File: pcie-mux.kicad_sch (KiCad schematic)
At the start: 0 parts

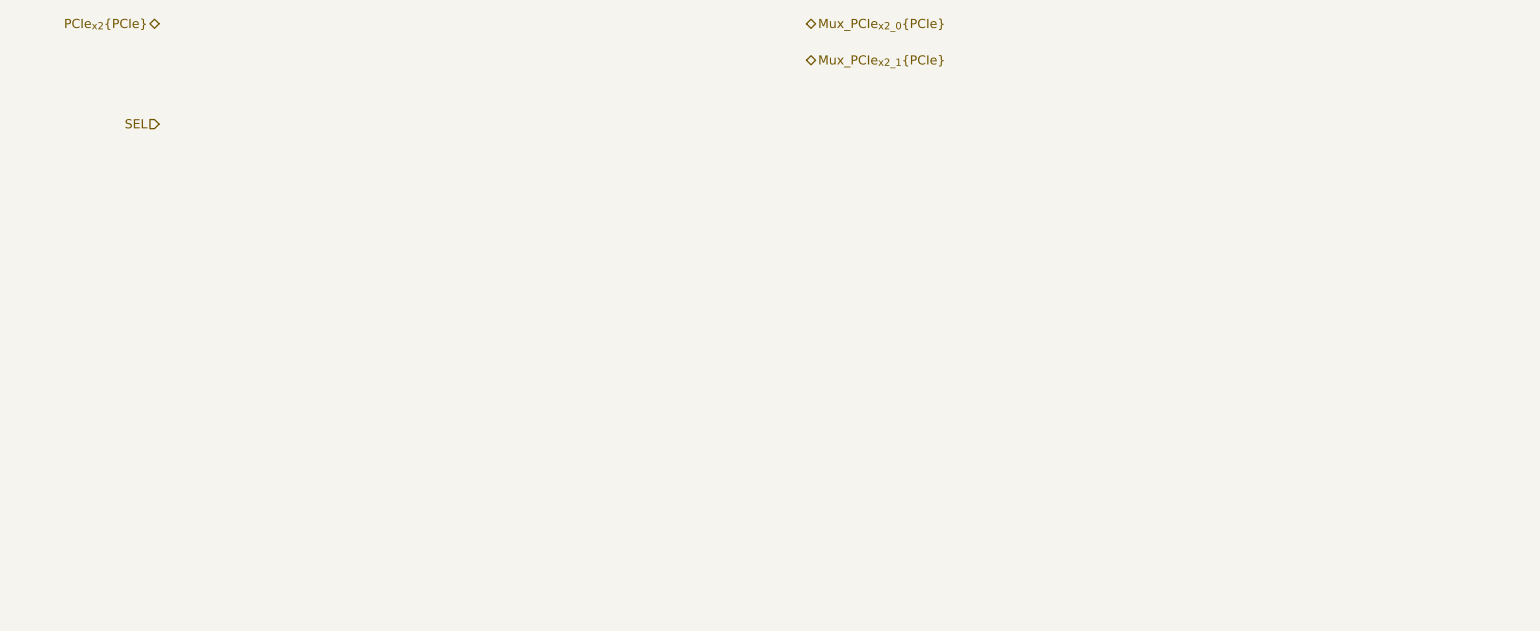
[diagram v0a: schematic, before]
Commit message: [#100765] Add JTAG for PCIe switch, add power pins
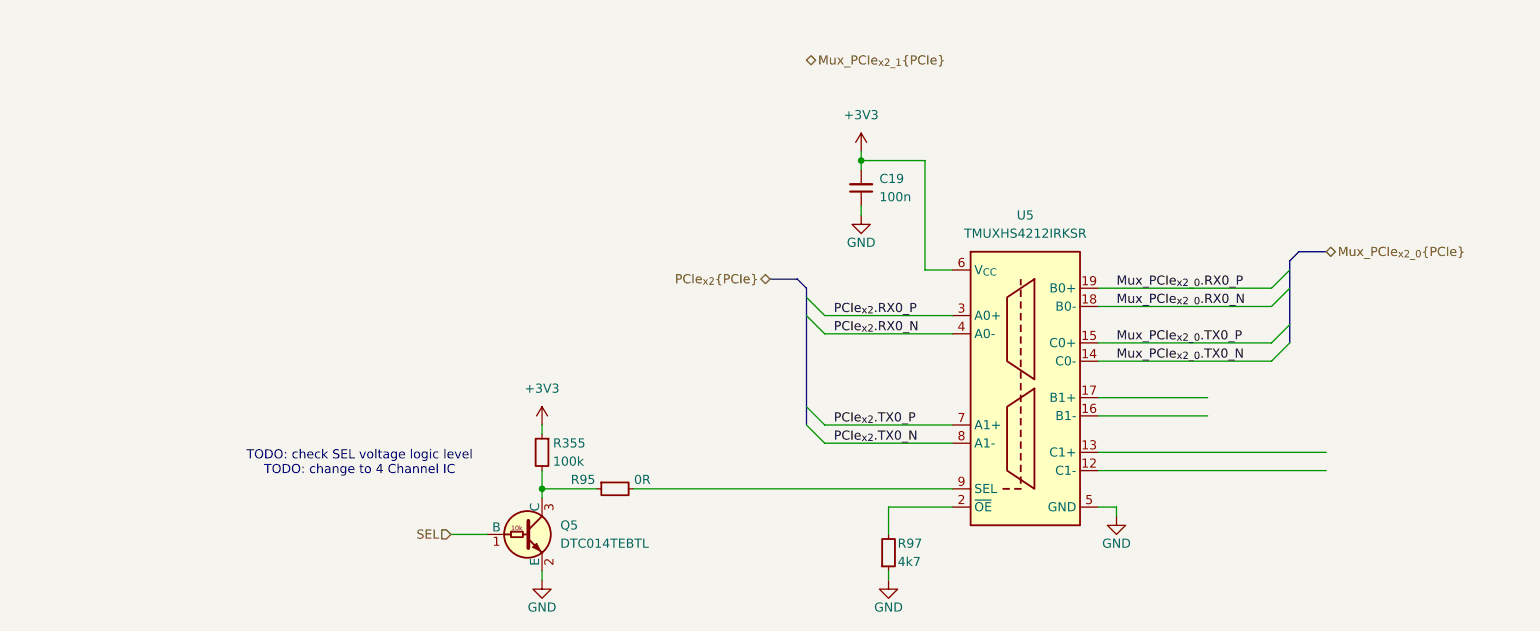
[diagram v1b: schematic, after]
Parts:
- added C19: C_100n_0402, antmicro-footprints:C_0402_1005Metric, symbol antmicroCapacitors0402:C_100n_0402
- added Q5: DTC014T_SOT-416, antmicro-footprints:SOT-416, symbol antmicroTransistorsBipolarSingle:DTC014T_SOT-416
- added R355: R_100k_0402, antmicro-footprints:R_0402_1005Metric, symbol antmicroResistors0402:R_100k_0402
- added R95: R_0R_0402, antmicro-footprints:R_0402_1005Metric, symbol antmicroResistors0402:R_0R_0402
- added R97: R_4k7_0402, antmicro-footprints:R_0402_1005Metric, symbol antmicroResistors0402:R_4k7_0402
- added U5: TMUXHS4212IRKSR, antmicro-footprints:VQFN-20_1EP_4.5x2.5mm_P0.5mm, symbol antmicroInterfaceAnalogSwitchesSpecialPurpose:TMUXHS4212IRKSR
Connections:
- net SEL: now also Q5.1 (B)
- new net: Q5.3 (C), R355.2, R95.1
- new net: R97.2, U5.2 (~{OE})
- new net: R95.2, U5.9 (SEL)
- new net +3V3: C19.2, R355.1, U5.6 (V_{CC})
- new net GND: C19.1, Q5.2 (E), R97.1, U5.11 (GND), U5.20 (GND), U5.21 (GND), U5.5 (GND)
- new net Mux_PCIe_{x2_0}.RX0_N: U5.18 (B0-)
- new net Mux_PCIe_{x2_0}.RX0_P: U5.19 (B0+)
- new net Mux_PCIe_{x2_0}.TX0_N: U5.14 (C0-)
- new net Mux_PCIe_{x2_0}.TX0_P: U5.15 (C0+)
- new net PCIe_{x2}.RX0_N: U5.4 (A0-)
- new net PCIe_{x2}.RX0_P: U5.3 (A0+)
- new net PCIe_{x2}.TX0_N: U5.8 (A1-)
- new net PCIe_{x2}.TX0_P: U5.7 (A1+)
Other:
- note added: "TODO: check SEL voltage logic level TODO: change to 4 Channel IC"

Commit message: [#100765] Work on schematic
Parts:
- removed C19: C_100n_0402, antmicro-footprints:C_0402_1005Metric, symbol antmicroCapacitors0402:C_100n_0402
- removed Q5: DTC014T_SOT-416, antmicro-footprints:SOT-416, symbol antmicroTransistorsBipolarSingle:DTC014T_SOT-416
- removed R355: R_100k_0402, antmicro-footprints:R_0402_1005Metric, symbol antmicroResistors0402:R_100k_0402
- removed R95: R_0R_0402, antmicro-footprints:R_0402_1005Metric, symbol antmicroResistors0402:R_0R_0402
- removed R97: R_4k7_0402, antmicro-footprints:R_0402_1005Metric, symbol antmicroResistors0402:R_4k7_0402
- removed U5: TMUXHS4212IRKSR, antmicro-footprints:VQFN-20_1EP_4.5x2.5mm_P0.5mm, symbol antmicroInterfaceAnalogSwitchesSpecialPurpose:TMUXHS4212IRKSR
- added C129, C130, C131: C_100n_0402, antmicro-footprints:C_0402_1005Metric, symbol antmicroCapacitors0402:C_100n_0402
- added Q6: DTC014T_SOT-416, antmicro-footprints:SOT-416, symbol antmicroTransistorsBipolarSingle:DTC014T_SOT-416
- added R218: R_0R_0402, antmicro-footprints:R_0402_1005Metric, symbol antmicroResistors0402:R_0R_0402
- added R220, R221: R_4k7_0402, antmicro-footprints:R_0402_1005Metric, symbol antmicroResistors0402:R_4k7_0402
- added R96: R_100k_0402, antmicro-footprints:R_0402_1005Metric, symbol antmicroResistors0402:R_100k_0402
- added U4: TMUXHS4412RUAR, antmicro-footprints:WQFN-42-1EP_3.5x9mm_P0.5mm, symbol antmicroInterfaceAnalogSwitchesSpecialPurpose:TMUXHS4412RUAR
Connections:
- net +3V3: now also C129.2, C130.2, C131.2, R96.1, U4.13 (VCC), U4.5 (VCC)
- net GND: now also C129.1, C130.1, C131.1, Q6.2 (E), R220.1, R221.1, U4.16 (GND), U4.21 (GND), U4.30 (GND), U4.39 (GND), U4.43 (GND), U4.6 (GND), U4.9 (GND)
- net Mux_PCIe_{x2_0}.RX0_N: now also U4.33 (DA1N)
- net Mux_PCIe_{x2_0}.RX0_P: now also U4.34 (DA1P)
- net Mux_PCIe_{x2_0}.TX0_N: now also U4.37 (DA0N)
- net Mux_PCIe_{x2_0}.TX0_P: now also U4.38 (DA0P)
- net PCIe_{x2}.RX0_N: now also U4.8 (D1N)
- net PCIe_{x2}.RX0_P: now also U4.7 (D1P)
- net PCIe_{x2}.TX0_N: now also U4.4 (D0N)
- net PCIe_{x2}.TX0_P: now also U4.3 (D0P)
- net SEL: now also Q6.1 (B)
- new net: Q6.3 (C), R218.1, R96.2
- new net: R218.2, U4.17 (SEL)
- new net: R221.2, U4.42 (RSVD)
- new net: R220.2, U4.18 (PD)
- new net Mux_PCIe_{x2_0}.RX1_N: U4.24 (DA3N)
- new net Mux_PCIe_{x2_0}.RX1_P: U4.25 (DA3P)
- new net Mux_PCIe_{x2_0}.TX1_N: U4.28 (DA2N)
- new net Mux_PCIe_{x2_0}.TX1_P: U4.29 (DA2P)
- new net Mux_PCIe_{x2_1}.RX0_N: U4.31 (DB1N)
- new net Mux_PCIe_{x2_1}.RX0_P: U4.32 (DB1P)
- new net Mux_PCIe_{x2_1}.RX1_N: U4.22 (DB3N)
- new net Mux_PCIe_{x2_1}.RX1_P: U4.23 (DB3P)
- new net Mux_PCIe_{x2_1}.TX0_N: U4.35 (DB0N)
- new net Mux_PCIe_{x2_1}.TX0_P: U4.36 (DB0P)
- new net Mux_PCIe_{x2_1}.TX1_N: U4.26 (DB2N)
- new net Mux_PCIe_{x2_1}.TX1_P: U4.27 (DB2P)
- new net PCIe_{x2_0}.RX1_N: U4.15 (D3N)
- new net PCIe_{x2_0}.RX1_P: U4.14 (D3P)
- new net PCIe_{x2_0}.TX1_N: U4.11 (D2N)
- new net PCIe_{x2_0}.TX1_P: U4.10 (D2P)
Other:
- note removed: "TODO: check SEL voltage logic level TODO: change to 4 Channel IC"

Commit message: [#100765] Update schematic
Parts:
- removed C129, C130, C131: C_100n_0402, antmicro-footprints:C_0402_1005Metric, symbol antmicroCapacitors0402:C_100n_0402
- removed Q6: DTC014T_SOT-416, antmicro-footprints:SOT-416, symbol antmicroTransistorsBipolarSingle:DTC014T_SOT-416
- removed R218: R_0R_0402, antmicro-footprints:R_0402_1005Metric, symbol antmicroResistors0402:R_0R_0402
- removed R96: R_100k_0402, antmicro-footprints:R_0402_1005Metric, symbol antmicroResistors0402:R_100k_0402
- added C1, C52, C53, C54, C55: C_100n_0402, antmicro-footprints:C_0402_1005Metric, symbol antmicroCapacitors0402:C_100n_0402
- added D6, D7: LED_G_0603_LG_L29K-G2J1-24-Z, antmicro-footprints:LED_0603_1608Metric_G, symbol antmicroLEDIndicationDiscrete:LED_G_0603_LG_L29K-G2J1-24-Z
- added Q4, Q5: BSS138PW,115, antmicro-footprints:SC70-3, symbol antmicroTransistorsFETsMOSFETsSingle:BSS138PW,115
- added R514, R515: R_470R_0402, antmicro-footprints:R_0402_1005Metric, symbol antmicroResistors0402:R_470R_0402
- added R52, R53, R54: R_10k_0402, antmicro-footprints:R_0402_1005Metric, symbol antmicroResistors0402:R_10k_0402
- added R55, R73, R74, R75, R76: R_0R_0402, antmicro-footprints:R_0402_1005Metric, symbol antmicroResistors0402:R_0R_0402
- added SW1: SW_CVS-02B, antmicro-footprints:SW_DIP_SPSTx02_Slide_Copal_CVS-02xB_W5.9mm_P1mm, symbol antmicroSlideSwitches:SW_CVS-02B
- added U11: SY75602BTWL-TR, antmicro-footprints:VDFN-8_1.6x1.4mm_P0.4mm, symbol antmicroClockTimingClockGeneratorsPLLsFrequencySynthesizers:SY75602BTWL-TR
- added U8: 74LVC1G157-Q100H_SOT457, antmicro-footprints:SC-74-6_1.5x2.9mm_P0.95mm, symbol antmicroInterfaceAnalogSwitchesMultiplexersDemultiplexers:74LVC1G157-Q100H_SOT4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
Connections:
- net +3V3: now also C1.2, C52.1, C53.1, C54.1, C55.1, D6.2 (A), D7.2 (A), R54.2, SW1.1, SW1.2, U11.8 (VDD), U8.5 (VCC)
- net GND: now also C1.1, C52.2, C53.2, C54.2, C55.2, Q4.2 (S), Q5.2 (S), R52.1, R53.1, SW1.5 (SH), U11.5 (GND), U8.2 (GND)
- net SEL: now also U8.3 (I0)
- net PCIE_{MUX_CH}: now reaches U4.17 (SEL)
- net PCIE_{MUX_CH}: now also Q4.1 (G), R55.2
- net PCIe_{x2_0}.RX1_N renamed PCIe_{x2}.RX1_N
- net PCIe_{x2_0}.RX1_P renamed PCIe_{x2}.RX1_P
- net PCIe_{x2_0}.TX1_N renamed PCIe_{x2}.TX1_N
- net PCIe_{x2_0}.TX1_P renamed PCIe_{x2}.TX1_P
- new net: R53.2, SW1.4, U8.1 (I1)
- new net: R55.1, U8.4 (Y)
- new net: Q4.3 (D), Q5.1 (G), R514.1, R54.1
- new net: D6.1 (C), R514.2
- new net: D7.1 (C), R515.2
- new net: Q5.3 (D), R515.1
- new net Mux_PCIe_{x2_0}.CLK_N: U11.4 (OUT0_N)
- new net Mux_PCIe_{x2_0}.CLK_P: U11.3 (OUT0_P)
- new net Mux_PCIe_{x2_0}.~{CLK_REQ}: R75.2
- new net Mux_PCIe_{x2_0}.~{RST}: R73.2
- new net Mux_PCIe_{x2_1}.CLK_N: U11.7 (OUT1_N)
- new net Mux_PCIe_{x2_1}.CLK_P: U11.6 (OUT1_P)
- new net Mux_PCIe_{x2_1}.~{CLK_REQ}: R76.2
- new net Mux_PCIe_{x2_1}.~{RST}: R74.2
- new net PCIe_{x2}.CLK_N: U11.2 (IN_N)
- new net PCIe_{x2}.CLK_P: U11.1 (IN_P)
- new net PCIe_{x2}.~{CLK_REQ}: R75.1, R76.1
- new net PCIe_{x2}.~{RST}: R73.1, R74.1
- new net SEL_MUX: R52.2, SW1.3, U8.6 (S)
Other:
- note added: "D6: OFF, D7: ON = PORT A"
- note added: "D6: ON, D7: OFF = PORT B"
- note added: "JOB_GPIO12"
- note added: "LED Status"
- note added: "PCIe Multiplexer"
- note added: "PCIe clock Multiplexer"
- moved on the sheet: R220, R221, U4

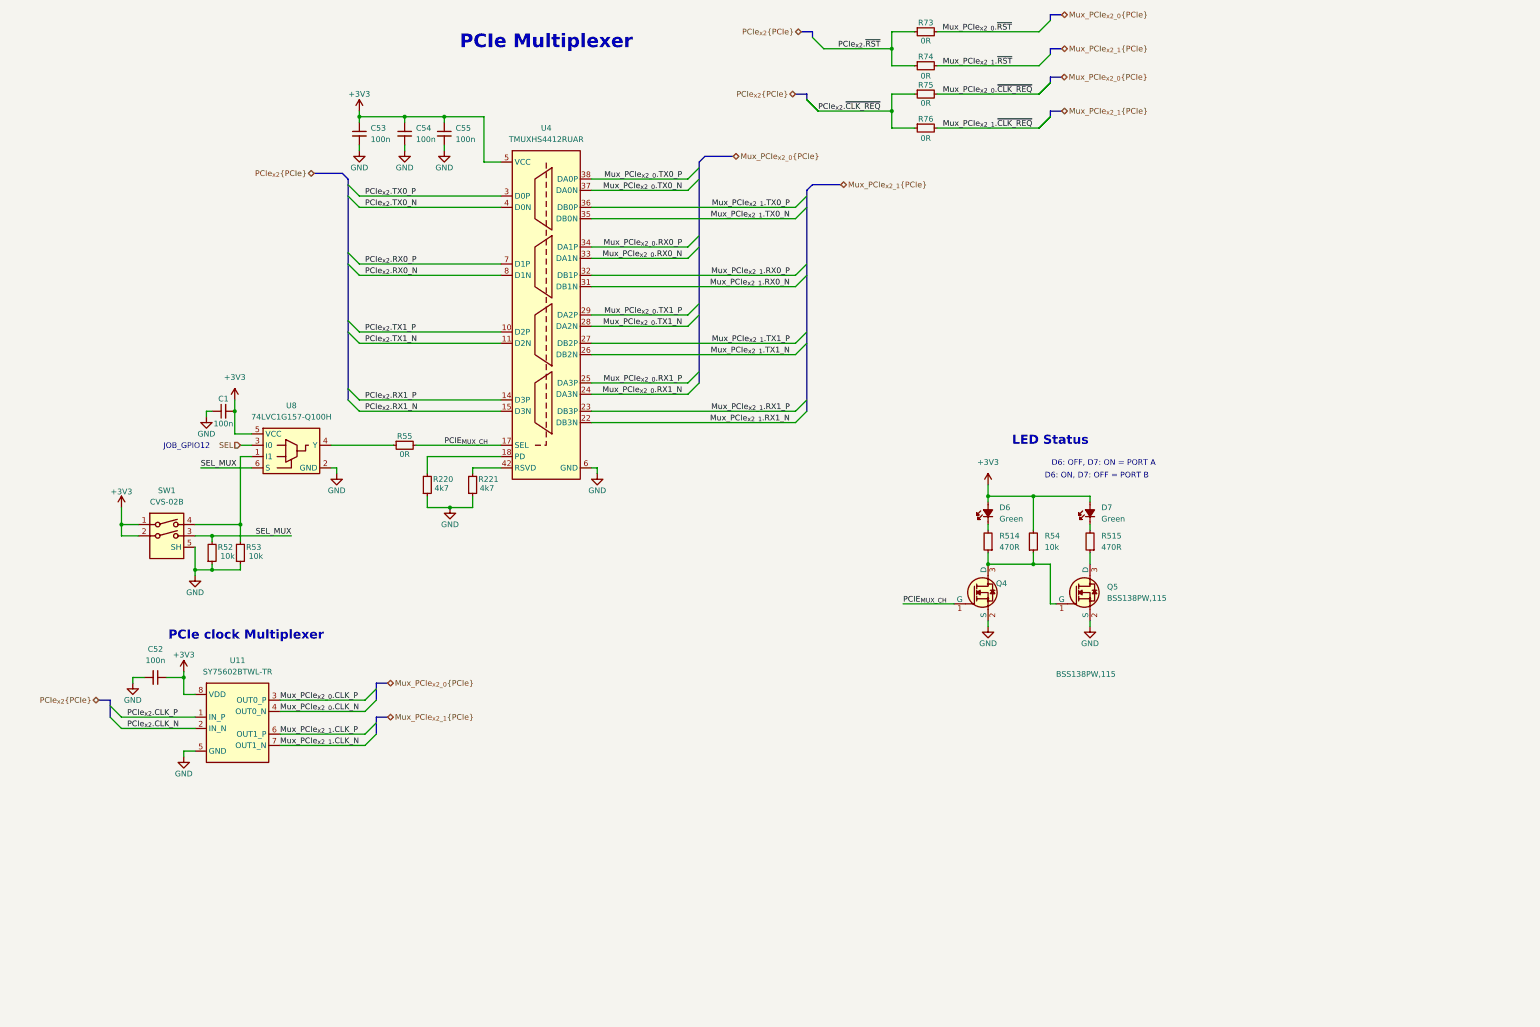
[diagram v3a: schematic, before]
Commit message: [#100765] Change sheet format to A3, update schematic
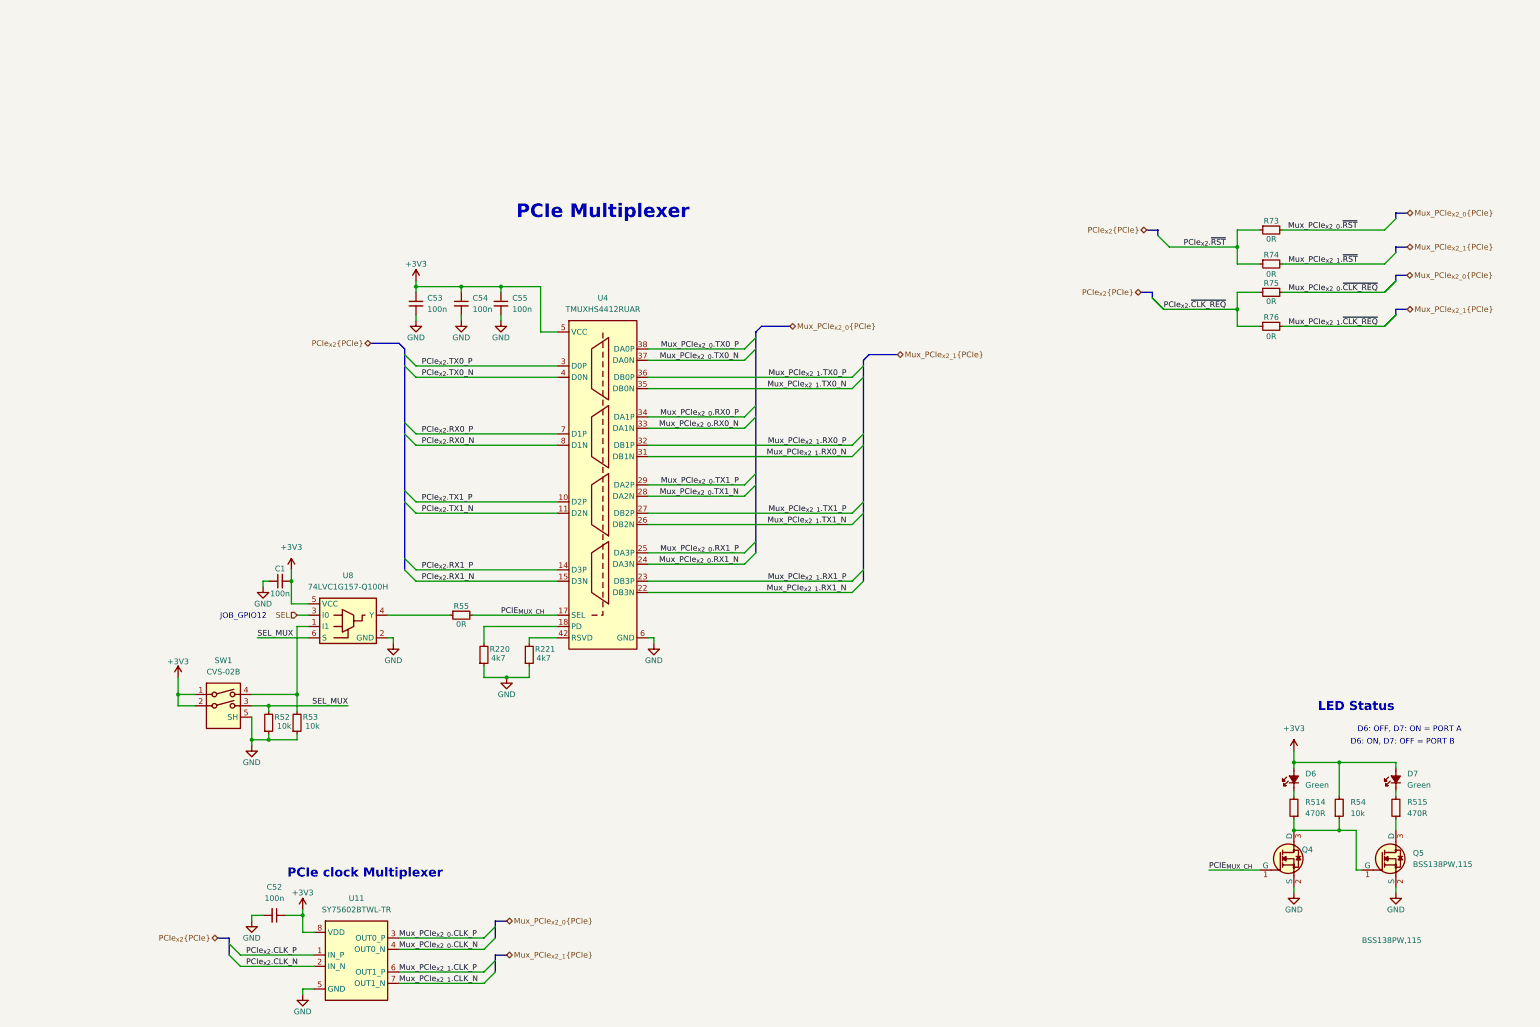
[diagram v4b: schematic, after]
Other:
- company: (none) -> Antmicro
- title: (none) -> antmicro-jetson-orin-baseboard-pcie-switch-expansion-hw
- moved on the sheet: C1, C52, C53, C54, C55, D6, D7, Q4, Q5, R220, R221, R514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
